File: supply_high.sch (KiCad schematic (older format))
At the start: 41 parts, among them Q21 BC817, U35 LM317L_SOT89, U36 LP2985-3.3, U37 TL432, U38 TC7660S, U39 LM337L_SO8

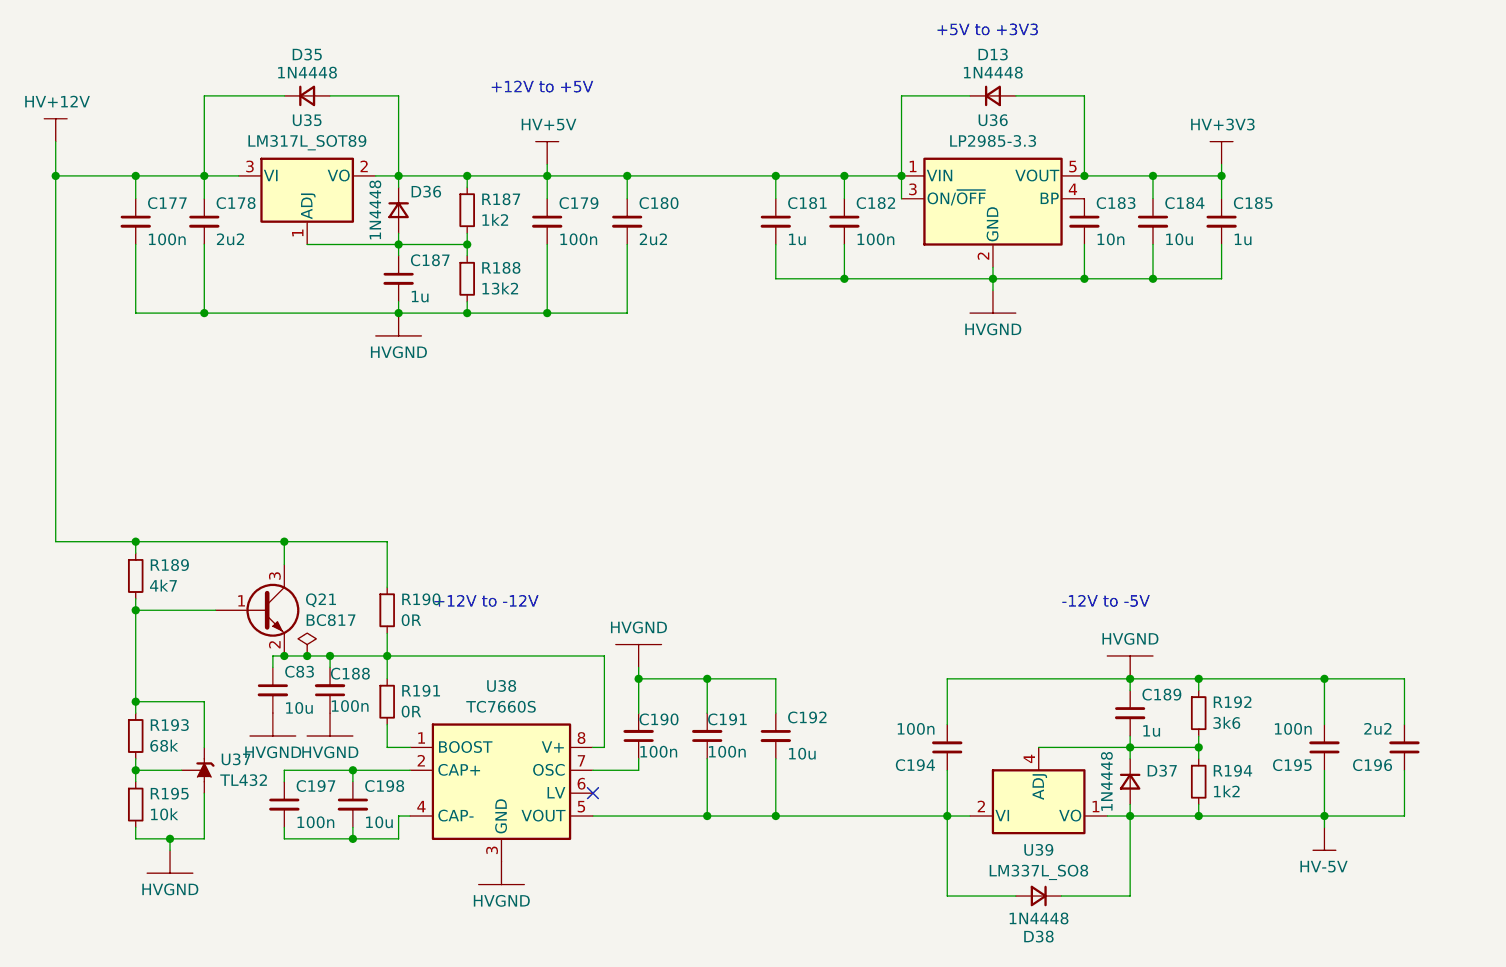
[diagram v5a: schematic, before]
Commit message: - as-built changes - add custom library elements
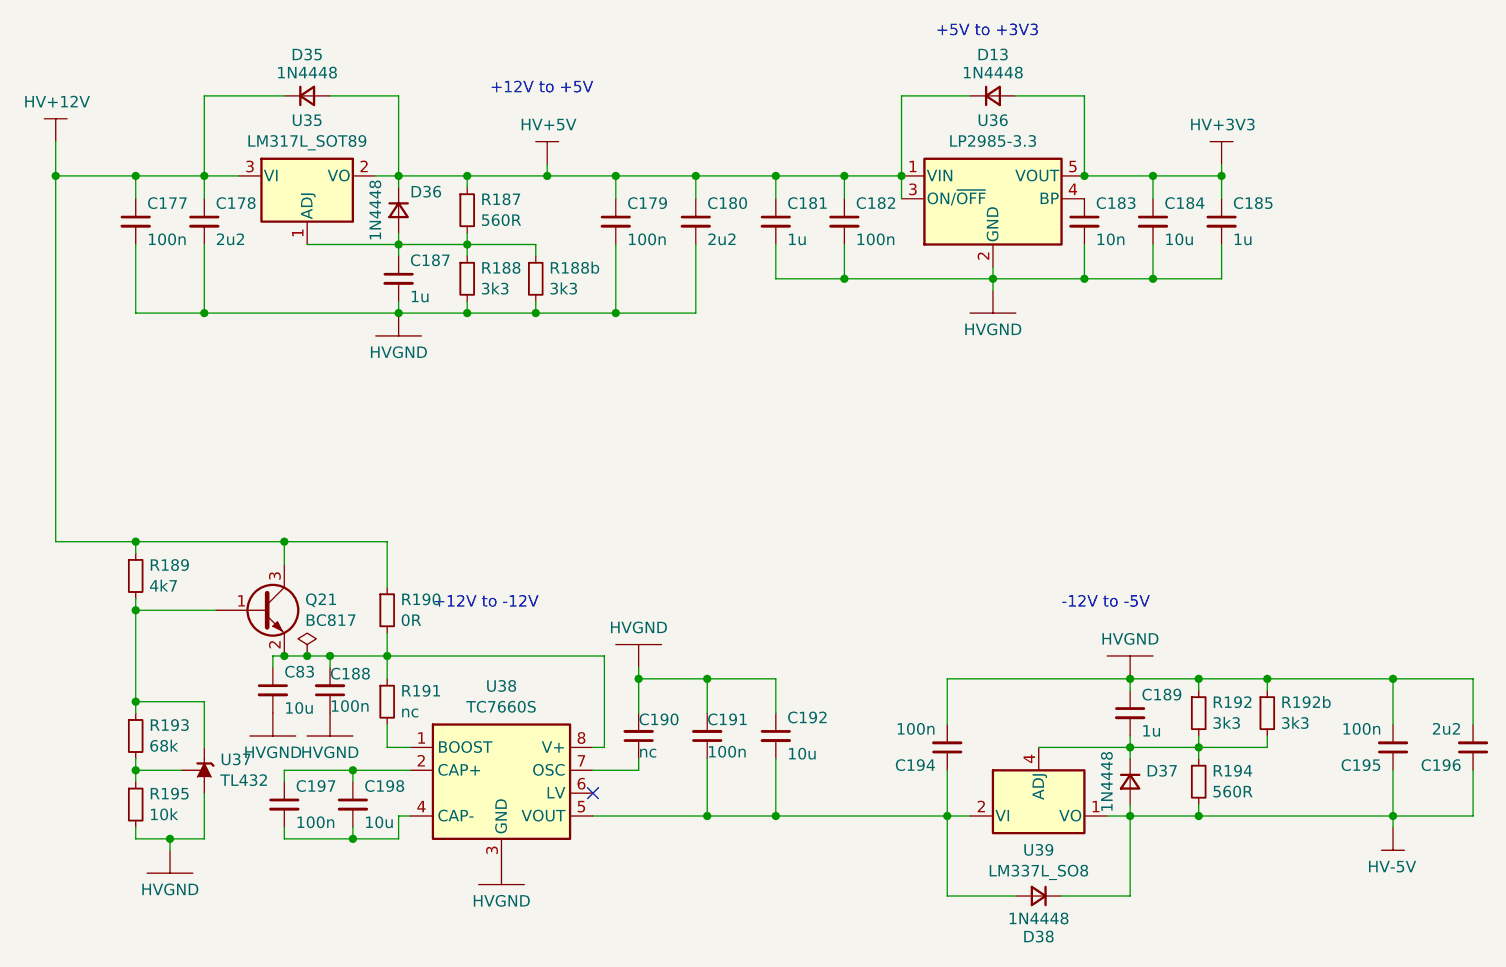
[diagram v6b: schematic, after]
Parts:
- added R188b: 3k3, Resistor_SMD:R_0603_1608Metric_Pad1.05x0.95mm_HandSolder, symbol Device:R_Small
- added R192b: 3k3, symbol Device:R_Small
- C190: value 100n -> nc
- R187, R194: value 1k2 -> 560R
- R188: value 13k2 -> 3k3
- R191: value 0R -> nc
- R192: value 3k6 -> 3k3
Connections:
- net HVGND: now also R188b.2, R192b.1
- net at C189.2, D37.1 (K), R192.2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: now also R192b.2
- net at C187.1, D36.2 (A), R187.2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: now also R188b.1
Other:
- moved on the sheet: C179, C180, C195, C196
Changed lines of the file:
@@
 $Descr A4 11693 8268
 encoding utf-8
-Sheet 11 10
-Title ""
-Date ""
-Rev ""
-Comp ""
+Sheet 10 10
+Title "Zasilanie - katoda"
+Date "2021-01-18"
+Rev "1.0"
+Comp "Łukasz Sitarek"
 Comment1 ""
 Comment2 ""
@@
 AR Path="/5FB035A9/5FB24FCD" Ref="R191"  Part="1"
 F 0 "R191" H 3809 4846 50  0000 L CNN
-F 1 "0R" H 3809 4755 50  0000 L CNN
+F 1 "nc" H 3809 4755 50  0000 L CNN
 F 2 "Resistor_SMD:R_0603_1608Metric" H 3750 4800 50  0001 C CNN
 F 3 "~" H 3750 4800 50  0001 C CNN
@@
 AR Path="/5FB035A9/5FB52DE1" Ref="C190"  Part="1"
 F 0 "C190" H 4850 4850 50  0000 R BNN
-F 1 "100n" H 4850 5050 50  0000 R TNN
+F 1 "nc" H 4850 5050 50  0000 R TNN
 F 2 "Capacitor_SMD:C_0603_1608Metric" H 4850 4950 50  0001 C CNN
 F 3 "~" H 4850 4950 50  0001 C CNN
@@
 L Device:C_Small C?
 U 1 1 5FB5BCAF
-P 8200 5000
+P 8500 5000
 AR Path="/5F620813/5FB5BCAF" Ref="C?"  Part="1"
 AR Path="/5F7A93EE/5FB5BCAF" Ref="C?"  Part="1"
 AR Path="/5FB035A9/5FB5BCAF" Ref="C196"  Part="1"
-F 0 "C196" H 8250 5050 50  0000 L BNN
-F 1 "2u2" H 8250 4950 50  0000 L TNN
-F 2 "Capacitor_SMD:C_0805_2012Metric" H 8200 5000 50  0001 C CNN
-F 3 "~" H 8200 5000 50  0001 C CNN
-	1    8200 5000
+F 0 "C196" H 8550 5050 50  0000 L BNN
+F 1 "2u2" H 8550 4950 50  0000 L TNN
+F 2 "Capacitor_SMD:C_0805_2012Metric" H 8500 5000 50  0001 C CNN
+F 3 "~" H 8500 5000 50  0001 C CNN
+	1    8500 5000
 	-1   0    0    1
 $EndComp
 Wire Wire Line
-	8200 5100 8200 5300
+	8500 5100 8500 5300
 $Comp
 L Device:C_Small C?
 U 1 1 5FB5BCC3
-P 7850 5000
+P 8150 5000
 AR Path="/5F620813/5FB5BCC3" Ref="C?"  Part="1"
 AR Path="/5FB035A9/5FB5BCC3" Ref="C195"  Part="1"
-F 0 "C195" H 7900 5050 50  0000 L BNN
-F 1 "100n" H 7900 4950 50  0000 L TNN
-F 2 "Capacitor_SMD:C_0603_1608Metric" H 7850 5000 50  0001 C CNN
-F 3 "~" H 7850 5000 50  0001 C CNN
-	1    7850 5000
+F 0 "C195" H 8200 5050 50  0000 L BNN
+F 1 "100n" H 8200 4950 50  0000 L TNN
+F 2 "Capacitor_SMD:C_0603_1608Metric" H 8150 5000 50  0001 C CNN
+F 3 "~" H 8150 5000 50  0001 C CNN
+	1    8150 5000
 	-1   0    0    1
 $EndComp
 Wire Wire Line
-	7850 5100 7850 5300
-Wire Wire Line
-	7300 5300 7850 5300
-Wire Wire Line
-	7850 5350 7850 5300
+	8150 5100 8150 5300
+Wire Wire Line
+	8150 5350 8150 5300
 $Comp
 L Device:D_Small D?
@@
 Wire Wire Line
 	6200 5300 6200 5650
-Connection ~ 7850 5300
+Connection ~ 8150 5300
 $Comp
 L Device:D_Small D?
@@
 $EndComp
 Wire Wire Line
-	8200 5300 7850 5300
+	8500 5300 8150 5300
 $Comp
 L Regulator_Linear:LM337L_SO8 U?
@@
 AR Path="/5FB035A9/5FB5BCF4" Ref="R192"  Part="1"
 F 0 "R192" H 7359 4896 50  0000 L CNN
-F 1 "3k6" H 7359 4805 50  0000 L CNN
+F 1 "3k3" H 7359 4805 50  0000 L CNN
 F 2 "Resistor_SMD:R_0603_1608Metric_Pad1.05x0.95mm_HandSolder" H 7300 4850 50  0001 C CNN
 F 3 "~" H 7300 4850 50  0001 C CNN
@@
 AR Path="/5FB035A9/5FB5BCFB" Ref="R194"  Part="1"
 F 0 "R194" H 7359 5196 50  0000 L CNN
-F 1 "1k2" H 7359 5105 50  0000 L CNN
+F 1 "560R" H 7359 5105 50  0000 L CNN
 F 2 "Resistor_SMD:R_0603_1608Metric_Pad1.05x0.95mm_HandSolder" H 7300 5150 50  0001 C CNN
 F 3 "~" H 7300 5150 50  0001 C CNN
@@
 Wire Wire Line
 	6300 5300 6200 5300
-Connection ~ 7300 5300
 $Comp
 L power_my:HVGND #PWR?
@@
 Connection ~ 7000 4700
 Wire Wire Line
-	7300 4700 7850 4700
-Wire Wire Line
-	8200 4700 8200 4900
-Connection ~ 7300 4700
-Wire Wire Line
-	7850 4900 7850 4700
-Connection ~ 7850 4700
-Wire Wire Line
-	7850 4700 8200 4700
+	8500 4700 8500 4900
+Wire Wire Line
+	8150 4900 8150 4700
+Connection ~ 8150 4700
+Wire Wire Line
+	8150 4700 8500 4700
 Wire Wire Line
 	7000 4700 6200 4700
@@
 L power_my:HV-5V #PWR0245
 U 1 1 5FB7C76F
-P 7850 5350
-F 0 "#PWR0245" H 7850 5200 50  0001 C CNN
-F 1 "HV-5V" H 7855 5523 50  0000 C CNN
-F 2 "" H 7850 5350 50  0001 C CNN
-F 3 "" H 7850 5350 50  0001 C CNN
-	1    7850 5350
+P 8150 5350
+F 0 "#PWR0245" H 8150 5200 50  0001 C CNN
+F 1 "HV-5V" H 8155 5523 50  0000 C CNN
+F 2 "" H 8150 5350 50  0001 C CNN
+F 3 "" H 8150 5350 50  0001 C CNN
+	1    8150 5350
 	-1   0    0    1
 $EndComp
@@
 	4450 2500 4450 2450
 Wire Wire Line
-	4450 2600 4450 2500
+	4750 2600 4750 2500
 Connection ~ 4450 2500
 $Comp
 L Device:C_Small C?
 U 1 1 5FB96CF8
-P 4800 2700
+P 5100 2700
 AR Path="/5F620813/5FB96CF8" Ref="C?"  Part="1"
 AR Path="/5F7A93EE/5FB96CF8" Ref="C?"  Part="1"
 AR Path="/5FB035A9/5FB96CF8" Ref="C180"  Part="1"
-F 0 "C180" H 4850 2750 50  0000 L BNN
-F 1 "2u2" H 4850 2650 50  0000 L TNN
-F 2 "Capacitor_SMD:C_0805_2012Metric" H 4800 2700 50  0001 C CNN
-F 3 "~" H 4800 2700 50  0001 C CNN
-	1    4800 2700
-	1    0    0    -1
-$EndComp
-Wire Wire Line
-	4800 2500 4800 2600
+F 0 "C180" H 5150 2750 50  0000 L BNN
+F 1 "2u2" H 5150 2650 50  0000 L TNN
+F 2 "Capacitor_SMD:C_0805_2012Metric" H 5100 2700 50  0001 C CNN
+F 3 "~" H 5100 2700 50  0001 C CNN
+	1    5100 2700
+	1    0    0    -1
+$EndComp
+Wire Wire Line
+	5100 2500 5100 2600
 $Comp
 L Device:C_Small C?
 U 1 1 5FB96D06
-P 4450 2700
+P 4750 2700
 AR Path="/5F620813/5FB96D06" Ref="C?"  Part="1"
 AR Path="/5FB035A9/5FB96D06" Ref="C179"  Part="1"
-F 0 "C179" H 4500 2750 50  0000 L BNN
-F 1 "100n" H 4500 2650 50  0000 L TNN
-F 2 "Capacitor_SMD:C_0603_1608Metric" H 4450 2700 50  0001 C CNN
-F 3 "~" H 4450 2700 50  0001 C CNN
-	1    4450 2700
+F 0 "C179" H 4800 2750 50  0000 L BNN
+F 1 "100n" H 4800 2650 50  0000 L TNN
+F 2 "Capacitor_SMD:C_0603_1608Metric" H 4750 2700 50  0001 C CNN
+F 3 "~" H 4750 2700 50  0001 C CNN
+	1    4750 2700
 	1    0    0    -1
 $EndComp
@@
 AR Path="/5FB035A9/5FB96D0D" Ref="R188"  Part="1"
 F 0 "R188" H 4159 2996 50  0000 L CNN
-F 1 "13k2" H 4159 2905 50  0000 L CNN
+F 1 "3k3" H 4159 2905 50  0000 L CNN
 F 2 "Resistor_SMD:R_0603_1608Metric_Pad1.05x0.95mm_HandSolder" H 4100 2950 50  0001 C CNN
 F 3 "~" H 4100 2950 50  0001 C CNN
@@
 AR Path="/5FB035A9/5FB96D14" Ref="R187"  Part="1"
 F 0 "R187" H 4159 2696 50  0000 L CNN
-F 1 "1k2" H 4159 2605 50  0000 L CNN
+F 1 "560R" H 4159 2605 50  0000 L CNN
 F 2 "Resistor_SMD:R_0603_1608Metric_Pad1.05x0.95mm_HandSolder" H 4100 2650 50  0001 C CNN
 F 3 "~" H 4100 2650 50  0001 C CNN
@@
 	3300 2150 2950 2150
 Wire Wire Line
-	4450 2500 4800 2500
+	4450 2500 4750 2500
 Wire Wire Line
 	2950 2150 2950 2500
@@
 Connection ~ 3800 3100
 Wire Wire Line
-	4100 3100 4450 3100
-Wire Wire Line
-	4450 3100 4450 2800
+	4750 3100 4750 2800
 Connection ~ 4100 3100
 Wire Wire Line
-	4450 3100 4800 3100
-Wire Wire Line
-	4800 3100 4800 2800
-Connection ~ 4450 3100
+	5100 3100 5100 2800
 Wire Wire Line
 	3800 3100 2950 3100
@@
 Wire Wire Line
 	5750 2950 6400 2950
-Wire Wire Line
-	4800 2500 5450 2500
-Connection ~ 4800 2500
 Text Notes 4200 2150 0    50   ~ 0
 +12V to +5V
@@
 	6800 2150 6800 2500
 Connection ~ 6800 2500
+$Comp
+L Device:R_Small R?
+U 1 1 5FD55DAB
+P 7600 4850
+AR Path="/5F620813/5FD55DAB" Ref="R?"  Part="1"
+AR Path="/5FB035A9/5FD55DAB" Ref="R192b"  Part="1"
+F 0 "R192b" H 7659 4896 50  0000 L CNN
+F 1 "3k3" H 7659 4805 50  0000 L CNN
+F 2 "" H 7600 4850 50  0001 C CNN
+F 3 "~" H 7600 4850 50  0001 C CNN
+	1    7600 4850
+	1    0    0    -1
+$EndComp
+Wire Wire Line
+	7300 5000 7600 5000
+Wire Wire Line
+	7600 5000 7600 4950
+Wire Wire Line
+	7300 4700 7600 4700
+Connection ~ 7300 4700
+Wire Wire Line
+	7600 4750 7600 4700
+Connection ~ 7600 4700
+Wire Wire Line
+	7600 4700 8150 4700
+Wire Wire Line
+	7300 5300 8150 5300
+Connection ~ 7300 5300
+$Comp
+L Device:R_Small R?
+U 1 1 5FD8634A
+P 4400 2950
+AR Path="/5F620813/5FD8634A" Ref="R?"  Part="1"
+AR Path="/5FB035A9/5FD8634A" Ref="R188b"  Part="1"
+F 0 "R188b" H 4459 2996 50  0000 L CNN
+F 1 "3k3" H 4459 2905 50  0000 L CNN
+F 2 "Resistor_SMD:R_0603_1608Metric_Pad1.05x0.95mm_HandSolder" H 4400 2950 50  0001 C CNN
+F 3 "~" H 4400 2950 50  0001 C CNN
+	1    4400 2950
+	1    0    0    -1
+$EndComp
+Connection ~ 4750 2500
+Connection ~ 4750 3100
+Connection ~ 5100 2500
+Wire Wire Line
+	5100 2500 5450 2500
+Wire Wire Line
+	4100 3100 4400 3100
+Wire Wire Line
+	4750 2500 5100 2500
+Wire Wire Line
+	4750 3100 5100 3100
+Wire Wire Line
+	4400 2850 4400 2800
+Wire Wire Line
+	4400 2800 4100 2800
+Wire Wire Line
+	4400 3050 4400 3100
+Connection ~ 4400 3100
+Wire Wire Line
+	4400 3100 4750 3100
 $EndSCHEMATC
